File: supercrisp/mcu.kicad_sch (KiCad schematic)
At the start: 13 parts, among them J1 SWD, P1 USB_C_Plug_USB2.0, SW27 SW_SPDT, U1 STM32F072CBTx, U2 USBLC6-2SC6, U6 TPS82140

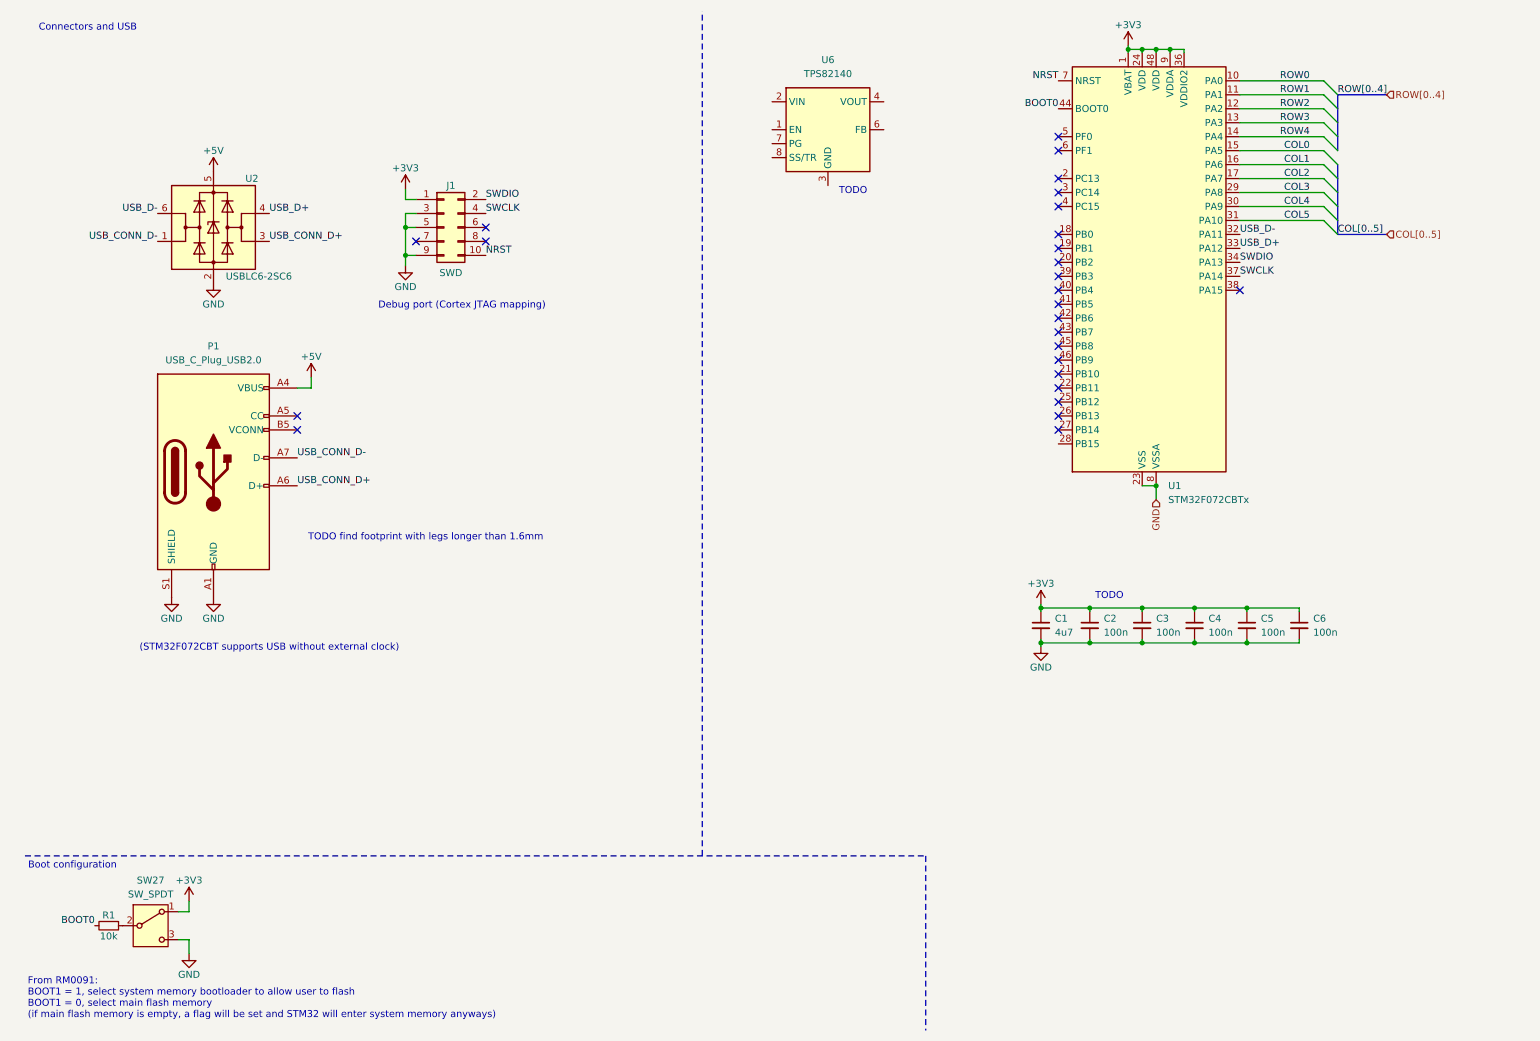
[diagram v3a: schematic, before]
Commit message: Add step down circuit in schematic editor
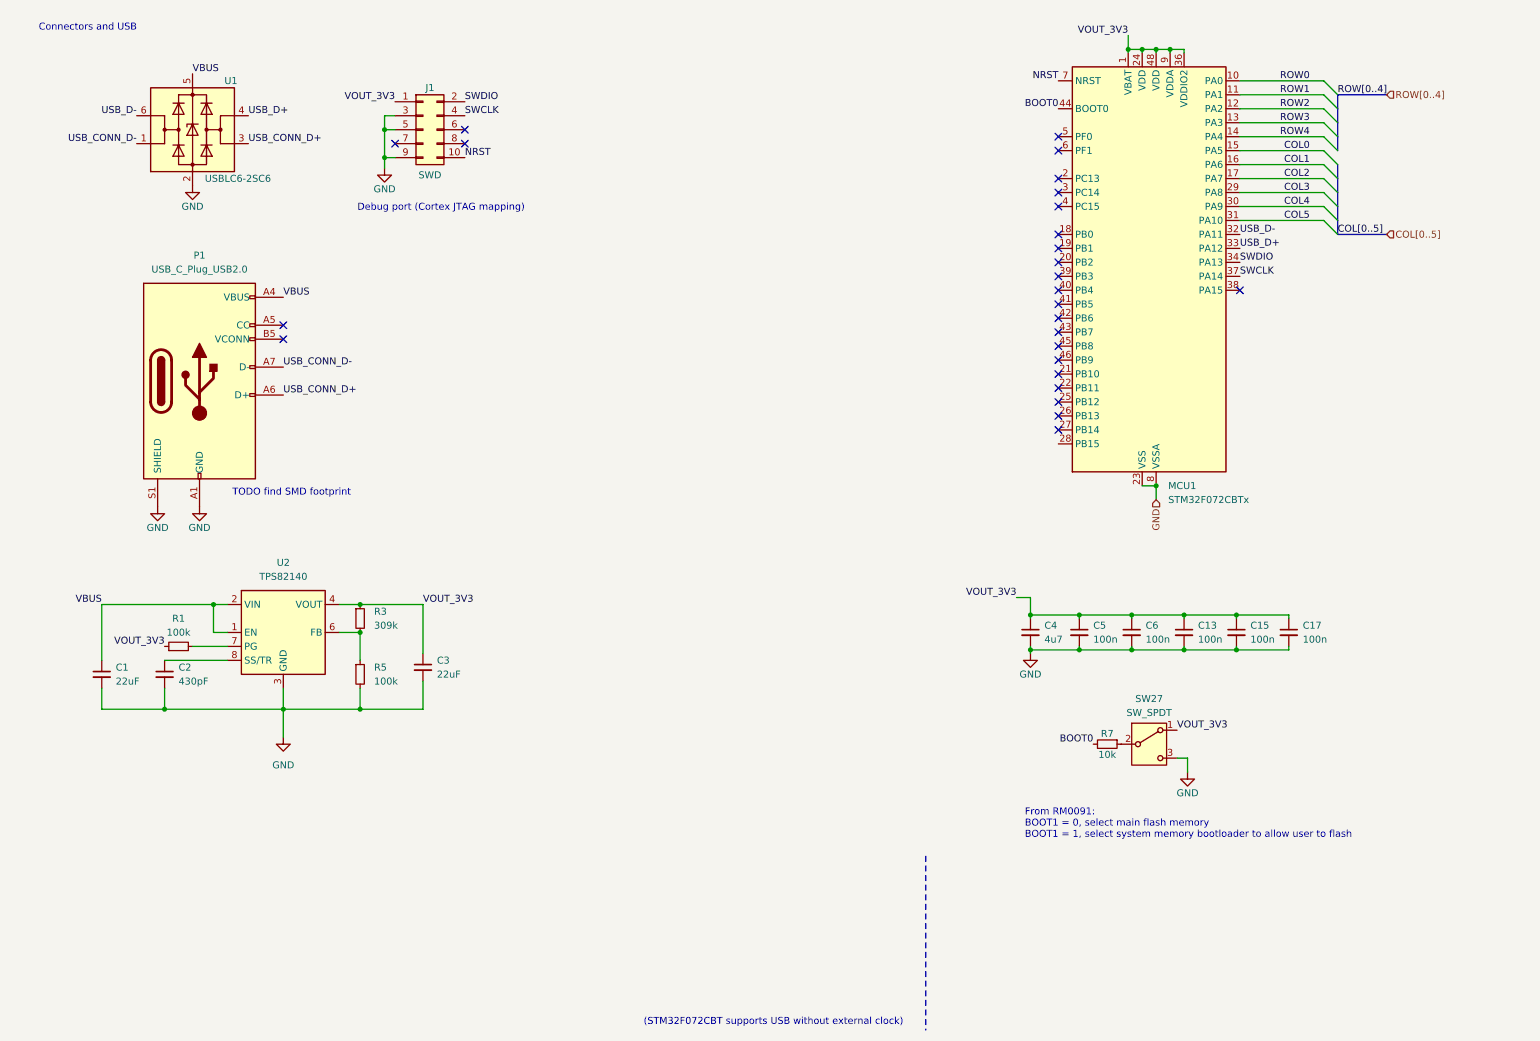
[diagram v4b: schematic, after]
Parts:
- removed U6: TPS82140, Package_LGA:Texas_SIL0008D_MicroSiP-8-1EP_2.8x3mm_P0.65mm_EP1.1x1.9mm_ThermalVias, symbol Regulator_Switching:TPS82140
- added C1, C3: 22uF, Capacitor_SMD:C_0603_1608Metric_Pad1.08x0.95mm_HandSolder, symbol Device:C_Small
- added C2: 430pF, Capacitor_SMD:C_0603_1608Metric_Pad1.08x0.95mm_HandSolder, symbol Device:C_Small
- added R1, R5: 100k, Resistor_SMD:R_0603_1608Metric, symbol Device:R_Small
- added R3: 309k, Resistor_SMD:R_0603_1608Metric, symbol Device:R_Small
- added U2: TPS82140, Package_LGA:Texas_SIL0008D_MicroSiP-8-1EP_2.8x3mm_P0.65mm_EP1.1x1.9mm_ThermalVias, symbol Regulator_Switching:TPS82140
- renumbered C4 to C13, C5 to C15, C6 to C17, C1 to C4, C2 to C5, C3 to C6, U1 to MCU1, R1 to R7, U2 to U1
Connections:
- net GND: now also C1.2, C2.2, C3.2, R5.2, U2.3 (GND), U2.9 (GND)
- net +3V3 renamed VOUT_3V3
- net VOUT_3V3: now also C3.1, R1.1, R3.1, U2.4 (VOUT), U2.5 (VOUT)
- net +5V renamed VBUS
- net VBUS: now also C1.1, U2.1 (EN), U2.2 (VIN)
- new net: C2.1, U2.8 (SS/TR)
- new net: R3.2, R5.1, U2.6 (FB)
- new net: R1.2, U2.7 (PG)
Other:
- note added: "From RM0091: BOOT1 = 0, select main flash memory BOOT1 = 1, select system memory bootloader to allow user to flash"
- note added: "TODO find SMD footprint"
- note removed: "Boot configuration"
- note removed: "From RM0091: BOOT1 = 1, select system memory bootloader to allow user to flash BOOT1 = 0, select main flash memory (if main flash memory is empty, a flag will be set and STM32 will enter system memory anyways)"
- note removed: "TODO"
- note removed: "TODO find footprint with legs longer than 1.6mm"
- moved on the sheet: C13, C15, C17, C4, C5, C6, J1, P1, R7, SW27, U1

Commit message: Continue placing components for USB
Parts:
- USB_P1: renamed from P1; JLCPCB Part # (none) -> C319148
- renumbered U2 to U1, U1 to USB_U1
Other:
- note added: "TODO find interface for wired split Avoid using TRSS preferably"
- note removed: "TODO find SMD footprint"

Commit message: Add pull down for USB CC
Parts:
- added R9: 5.1k, Resistor_SMD:R_0603_1608Metric, symbol Device:R_Small
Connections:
- net GND: now also R9.2
- net at USB_P1.A5 (CC): now also R9.1
- no-connect marks 26 -> 25
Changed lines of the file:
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@@
 	)
 	(no_connect
-		(at 59.69 69.85)
-	)
-	(no_connect
 		(at 200.66 63.5)
 	)
@@
 	(symbol
 		(lib_id "STM32F4_REV2-rescue:GND-power")
+		(at 64.77 69.85 90)
+		(unit 1)
+		(exclude_from_sim no)
+		(in_bom yes)
+		(on_board yes)
+		(dnp no)
+		(property "Reference" "#PWR018"
+			(at 71.12 69.85 0)
+			(effects
+				(font
+					(size 1.27 1.27)
+				)
+				(hide yes)
+			)
+		)
+		(property "Value" "GND"
+			(at 68.58 69.85 0)
+			(effects
+				(font
+					(size 1.27 1.27)
+				)
+			)
+		)
+		(property "Footprint" ""
+			(at 64.77 69.85 0)
+			(effects
+				(font
+					(size 1.27 1.27)
+				)
+				(hide yes)
+			)
+		)
+		(property "Datasheet" ""
+			(at 64.77 69.85 0)
+			(effects
+				(font
+					(size 1.27 1.27)
+				)
+				(hide yes)
+			)
+		)
+		(property "Description" ""
+			(at 64.77 69.85 0)
+			(effects
+				(font
+					(size 1.27 1.27)
+				)
+				(hide yes)
+			)
+		)
+		(pin "1"
+		)
+		(instances
+			(project "supercrisp"
+				(path "/623f70b3-6381-43ff-98c1-e36c34bee313/e058b5b4-db4d-4bc7-8f42-8e3bd37c89bf"
+					(reference "#PWR018")
+					(unit 1)
+				)
+				(path "/623f70b3-6381-43ff-98c1-e36c34bee313/c14a50ad-c630-40dd-ac14-b3b40c9c245d"
+					(reference "#PWR019")
+					(unit 1)
+				)
+			)
+		)
+	)
+	(symbol
+		(lib_id "STM32F4_REV2-rescue:GND-power")
 		(at 44.45 102.87 0)
 		(unit 1)
@@
 					(unit 1)
 				)
+			)
+		)
+	)
+	(symbol
+		(lib_id "Device:R_Small")
+		(at 62.23 69.85 90)
+		(unit 1)
+		(exclude_from_sim no)
+		(in_bom yes)
+		(on_board yes)
+		(dnp no)
+		(fields_autoplaced yes)
+		(property "Reference" "R9"
+			(at 62.23 64.77 90)
+			(effects
+				(font
+					(size 1.27 1.27)
+				)
+			)
+		)
+		(property "Value" "5.1k"
+			(at 62.23 67.31 90)
+			(effects
+				(font
+					(size 1.27 1.27)
+				)
+			)
+		)
+		(property "Footprint" "Resistor_SMD:R_0603_1608Metric"
+			(at 62.23 69.85 0)
+			(effects
+				(font
+					(size 1.27 1.27)
+				)
+				(hide yes)
+			)
+		)
+		(property "Datasheet" "~"
+			(at 62.23 69.85 0)
+			(effects
+				(font
+					(size 1.27 1.27)
+				)
+				(hide yes)
+			)
+		)
+		(property "Description" "Resistor, small symbol"
+			(at 62.23 69.85 0)
+			(effects
+				(font
+					(size 1.27 1.27)
+				)
+				(hide yes)
+			)
+		)
+		(property "JLCPCB Part #" ""
+			(at 62.23 69.85 0)
+			(effects
+				(font
+					(size 1.27 1.27)
+				)
+				(hide yes)
+			)
+		)
+		(pin "2"
+		)
+		(pin "1"
+		)
+		(instances
+			(project "supercrisp"
+				(path "/623f70b3-6381-43ff-98c1-e36c34bee313/e058b5b4-db4d-4bc7-8f42-8e3bd37c89bf"
+					(reference "R9")
+					(unit 1)
+				)
+				(path "/623f70b3-6381-43ff-98c1-e36c34bee313/c14a50ad-c630-40dd-ac14-b3b40c9c245d"
+					(reference "R10")
+					(unit 1)
+				)

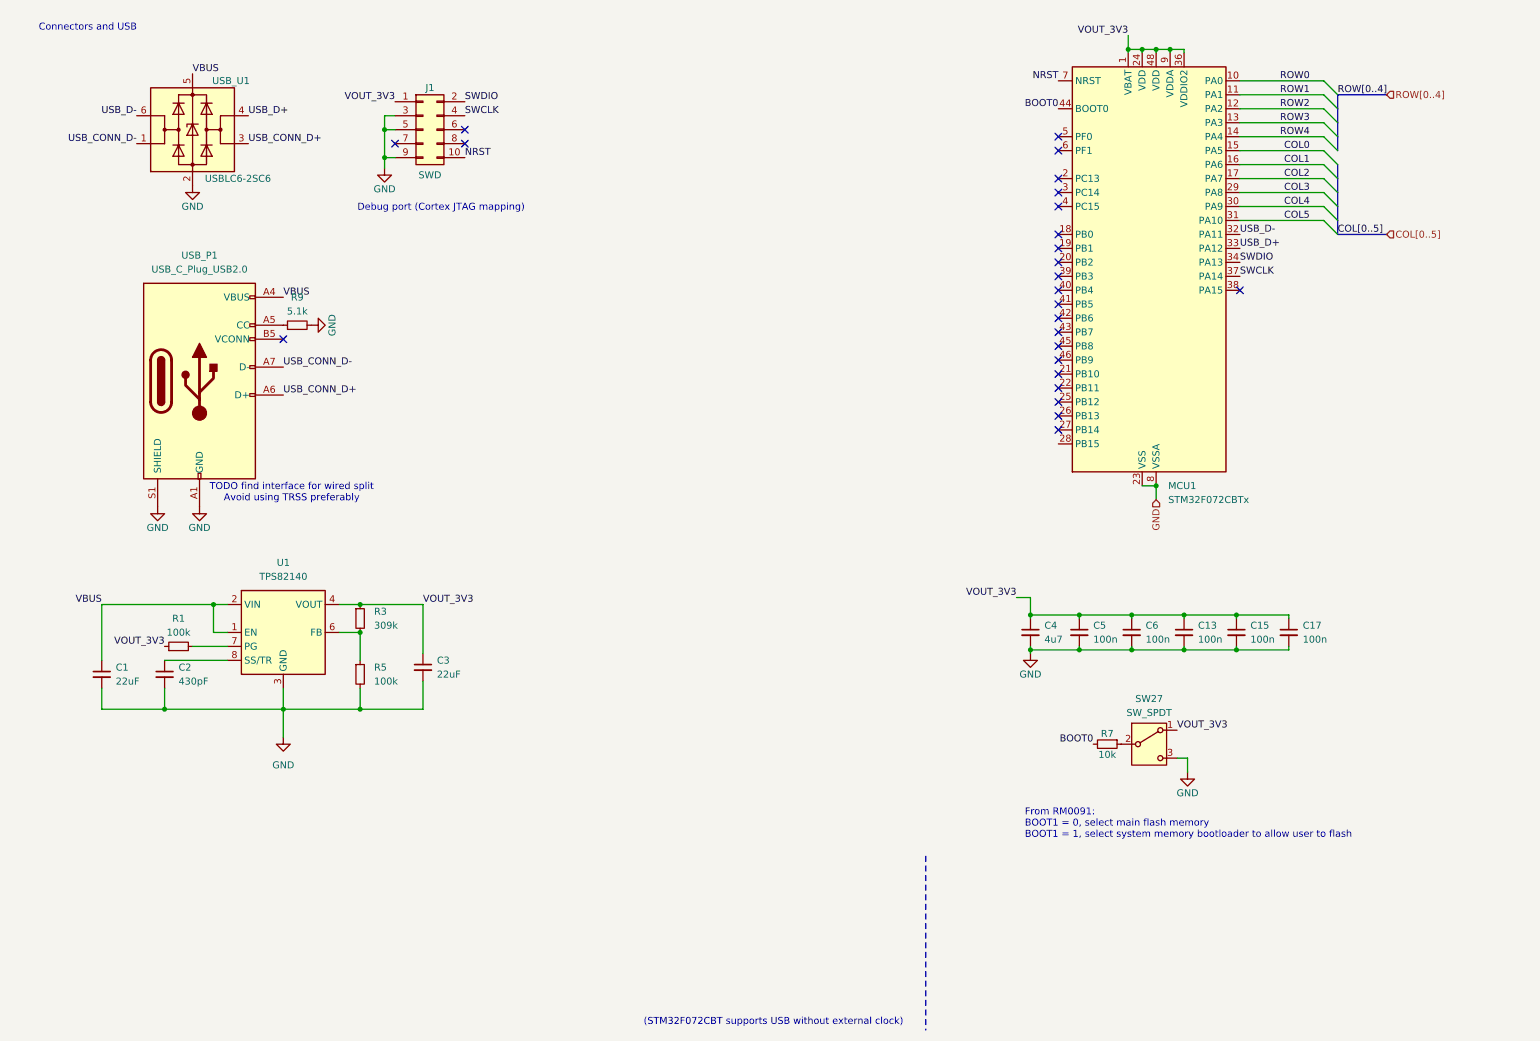
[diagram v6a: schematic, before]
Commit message: Add TRRS connector for serial communication between splits
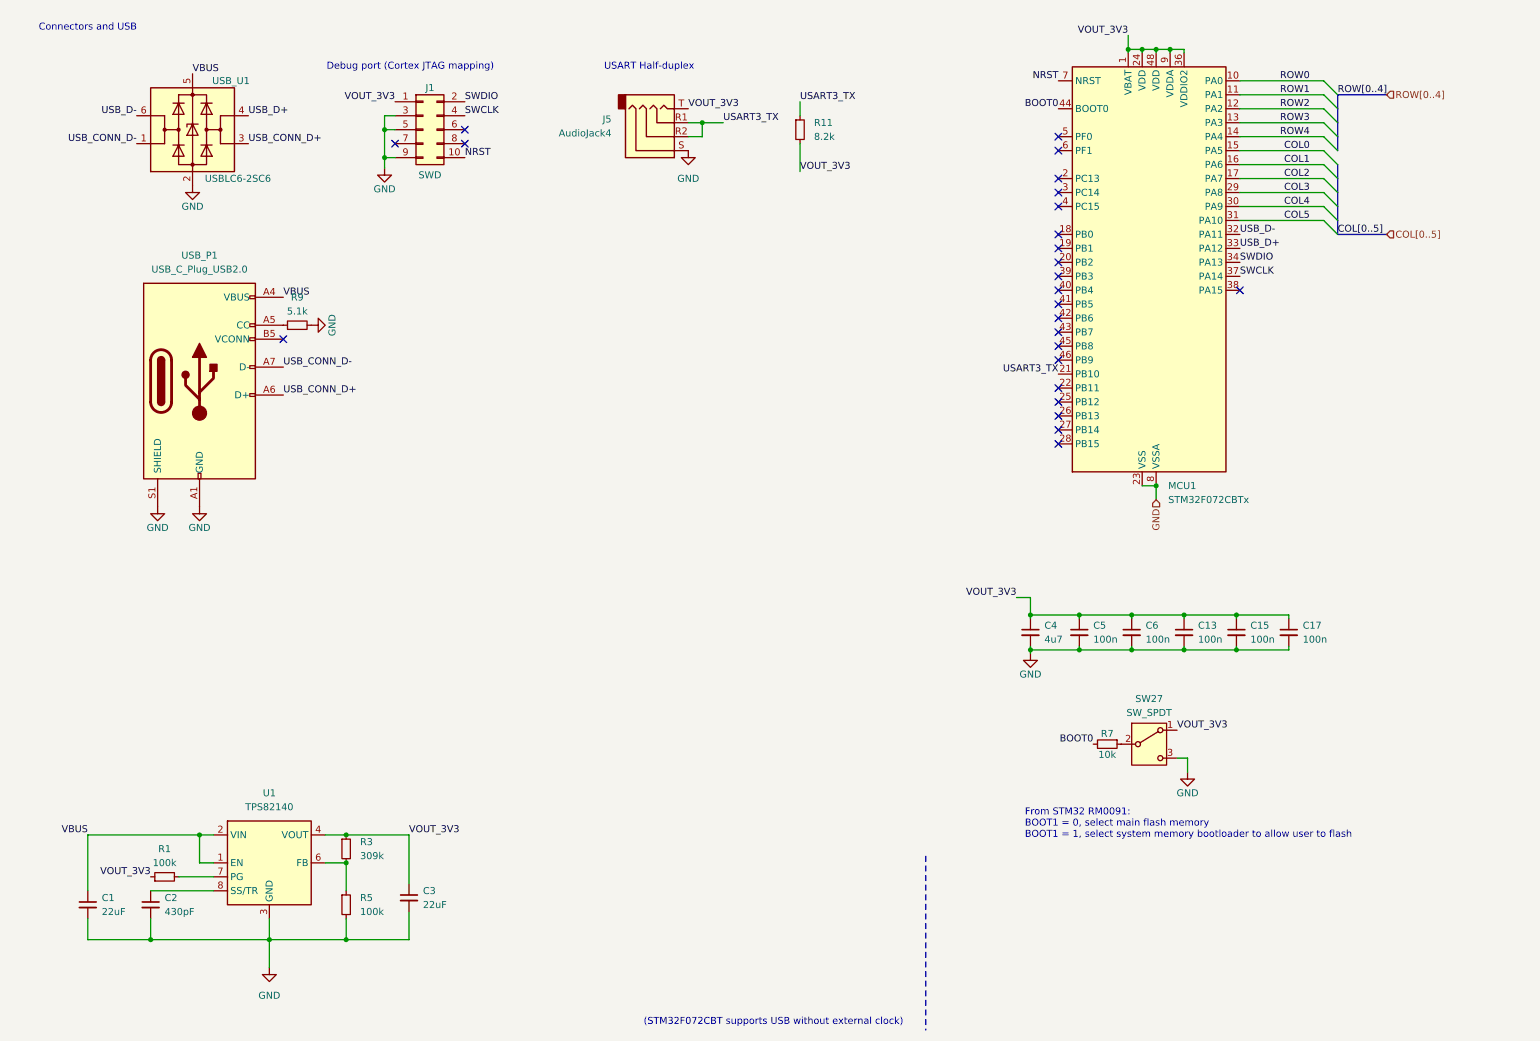
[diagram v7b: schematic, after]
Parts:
- added J5: AudioJack4, Connector_Audio:Jack_3.5mm_PJ320D_Horizontal, symbol Connector_Audio:AudioJack4
- added R11: 8.2k, Resistor_SMD:R_0603_1608Metric, symbol Device:R_Small
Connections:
- net GND: now also J5.S
- net VOUT_3V3: now also J5.T, R11.2
- net USART3_TX: now reaches MCU1.21 (PB10)
- net USART3_TX: now also J5.R1, J5.R2, R11.1
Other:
- note added: "From STM32 RM0091: BOOT1 = 0, select main flash memory BOOT1 = 1, select system memory bootloader to allow user to flash"
- note added: "USART Half-duplex"
- note removed: "From RM0091: BOOT1 = 0, select main flash memory BOOT1 = 1, select system memory bootloader to allow user to flash"
- note removed: "TODO find interface for wired split Avoid using TRSS preferably"
- moved on the sheet: C1, C2, C3, R1, R3, R5, U1

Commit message: WIP 0 errors, 58 warnings
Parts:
- removed C1, C3: 22uF, Capacitor_SMD:C_0603_1608Metric_Pad1.08x0.95mm_HandSolder, symbol Device:C_Small
- removed C2: 430pF, Capacitor_SMD:C_0603_1608Metric_Pad1.08x0.95mm_HandSolder, symbol Device:C_Small
- removed R1, R5: 100k, Resistor_SMD:R_0603_1608Metric, symbol Device:R_Small
- removed R3: 309k, Resistor_SMD:R_0603_1608Metric, symbol Device:R_Small
- removed U1: TPS82140, Package_LGA:Texas_SIL0008D_MicroSiP-8-1EP_2.8x3mm_P0.65mm_EP1.1x1.9mm_ThermalVias, symbol Regulator_Switching:TPS82140
- removed USB_U1: USBLC6-2SC6, Package_TO_SOT_SMD:SOT-23-6, symbol STM32F4_REV2-rescue:USBLC6-2SC6-Power_Protection
- MCU1: JLCPCB Part # (none) -> C81720
- USB_P1: JLCPCB Part # C319148 -> C319148
- renumbered C13 to C7, C15 to C8, C17 to C9, J5 to J4, R9 to R2, R11 to R5, R7 to R6, SW27 to SW1
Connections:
- net USB_CONN_D+ renamed USB_CONN_DP
- net USB_CONN_D- renamed USB_CONN_DN
- net USB_D+ renamed USB_DP
- net USB_D- renamed USB_DN
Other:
- note added: "Configure as open-drain mode"
- note added: "Easier to route between top & bottom layers when splits are inter-connected"
- moved on the sheet: R2, USB_P1
